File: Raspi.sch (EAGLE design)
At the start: 4 parts

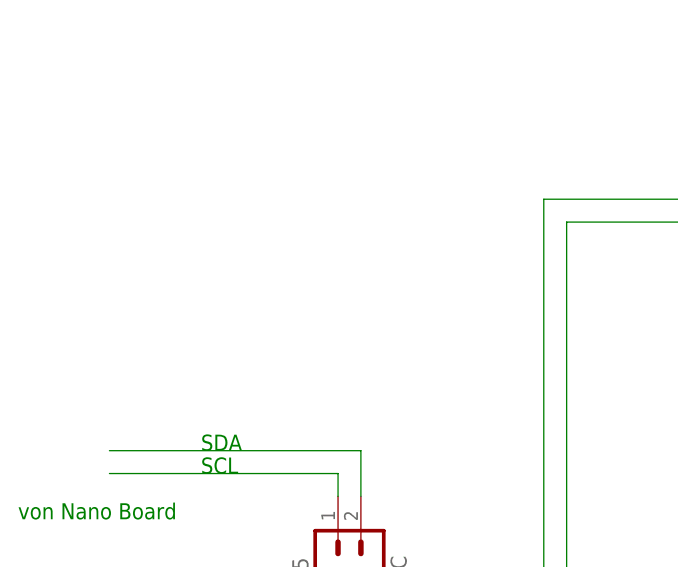
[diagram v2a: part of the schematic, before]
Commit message: 
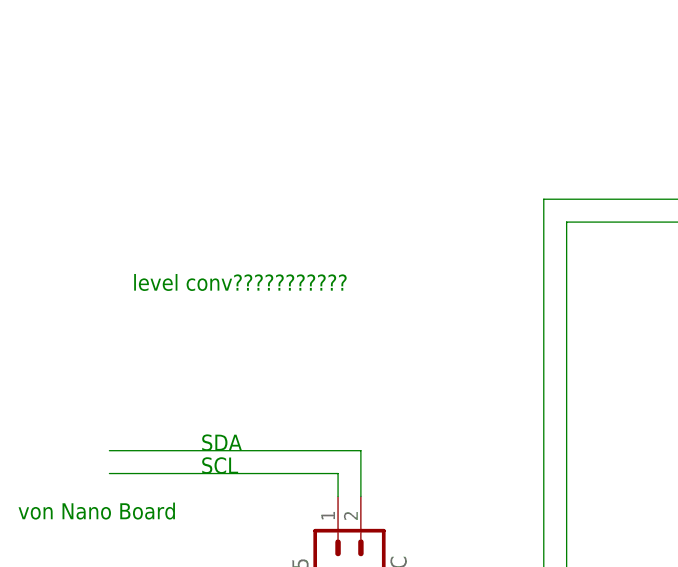
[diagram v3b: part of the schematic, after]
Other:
- note added: "level conv???????????"
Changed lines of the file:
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@@
 <text x="134.62" y="160.02" size="1.778" layer="91" rot="R180">motRechts rückw</text>
 <text x="134.62" y="157.48" size="1.778" layer="91" rot="R180">motRechts PWM</text>
+<text x="-10.16" y="165.1" size="1.778" layer="91">level conv???????????</text>
 </plain>
 <instances>

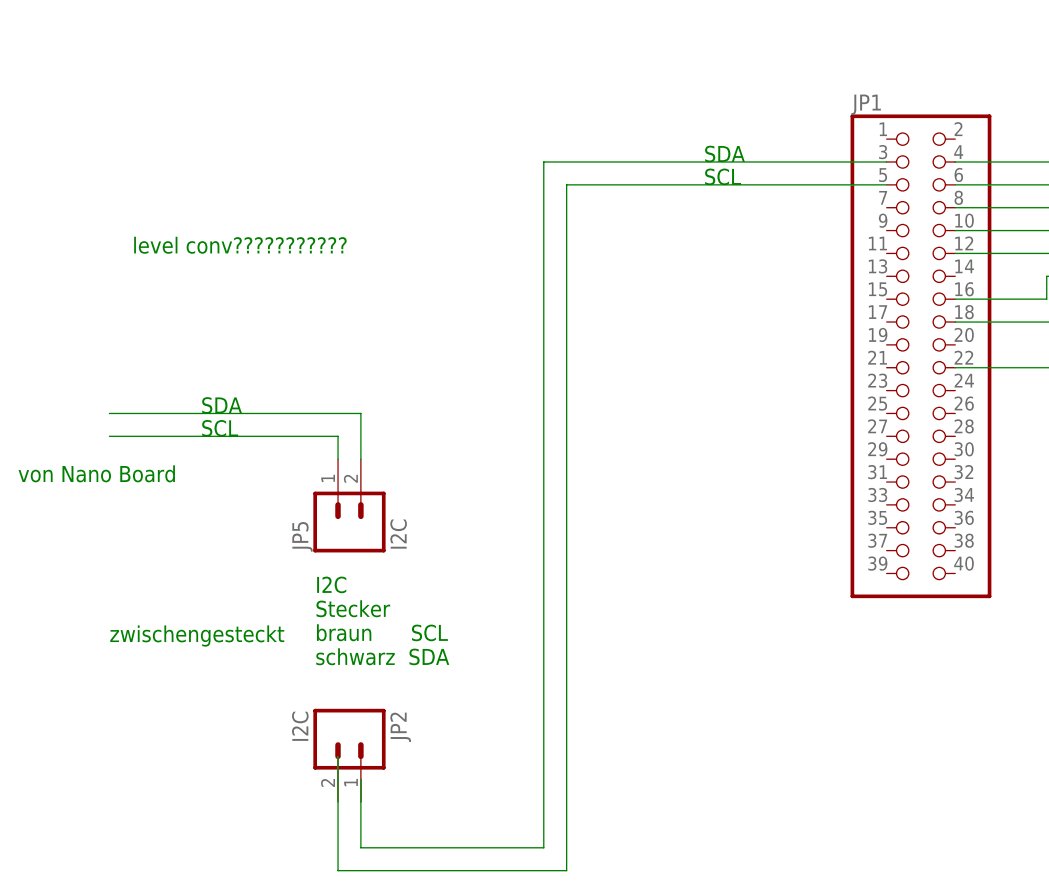
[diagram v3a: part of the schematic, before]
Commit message: 
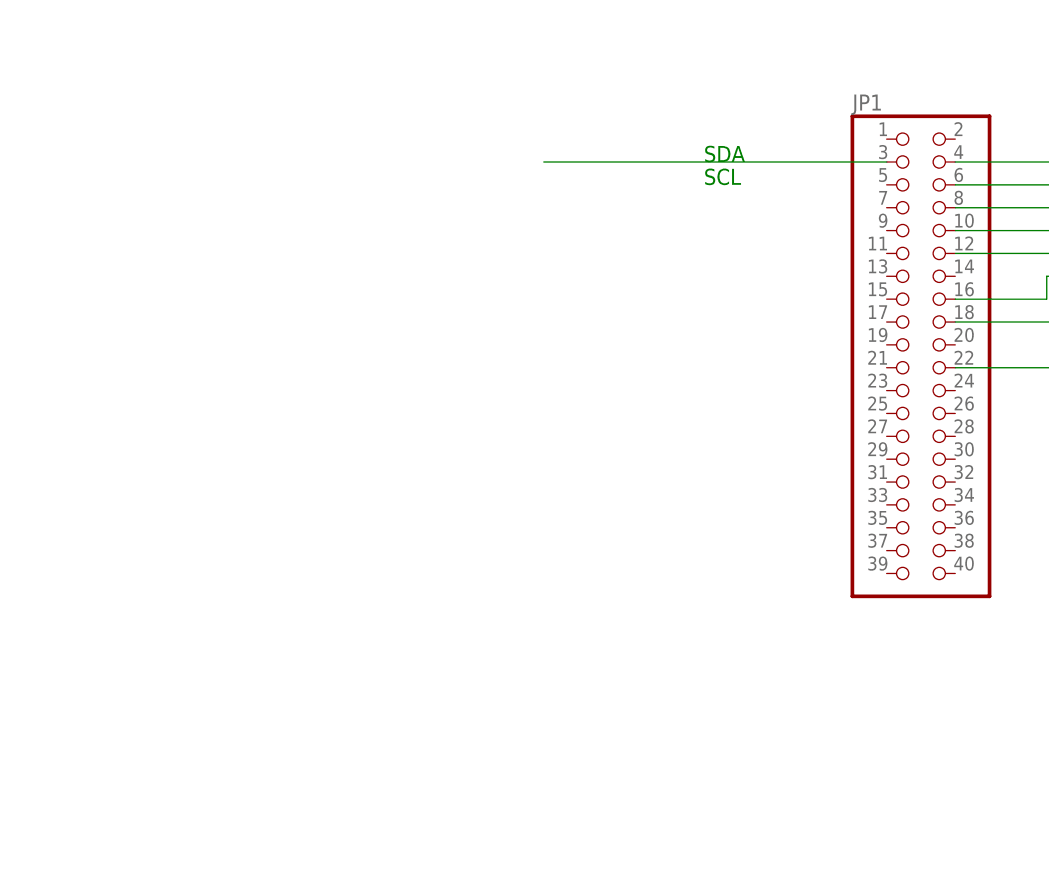
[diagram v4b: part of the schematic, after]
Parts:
- removed JP2, JP5: I2C, SparkFun-Connectors:M02-JST-2MM-SMT
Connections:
- removed net N$10: JP5.2
- removed net N$11: JP5.1
- removed net N$2: JP1.5
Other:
- note removed: "I2C Stecker braun SCL schwarz SDA"
- note removed: "level conv???????????"
- note removed: "von Nano Board"
- note removed: "zwischengesteckt"
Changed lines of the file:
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@@
 <part name="FRAME1" library="SparkFun-Aesthetics" deviceset="FRAME-A4L" device=""/>
 <part name="JP1" library="adafruit" deviceset="PINHD-2X20" device=""/>
-<part name="JP5" library="SparkFun-Connectors" deviceset="M02" device="-JST-2MM-SMT" value="I2C"/>
-<part name="JP2" library="SparkFun-Connectors" deviceset="M02" device="-JST-2MM-SMT" value="I2C"/>
 <part name="JP3" library="SparkFun-Connectors" deviceset="M06" device="LOCK" value="Motorregler"/>
 </parts>
@@
 <sheet>
 <plain>
-<text x="-2.54" y="144.78" size="1.778" layer="91">SCL</text>
-<text x="-2.54" y="147.32" size="1.778" layer="91">SDA</text>
-<text x="10.16" y="119.38" size="1.778" layer="91">I2C
-Stecker
-braun      SCL
-schwarz  SDA</text>
 <text x="53.34" y="175.26" size="1.778" layer="91">SDA</text>
 <text x="53.34" y="172.72" size="1.778" layer="91">SCL</text>
-<text x="-22.86" y="139.7" size="1.778" layer="91">von Nano Board</text>
-<text x="-12.7" y="121.92" size="1.778" layer="91">zwischengesteckt</text>
 <text x="91.44" y="205.74" size="1.778" layer="91">5V</text>
 <text x="96.52" y="205.74" size="1.778" layer="91">GND</text>
@@
 <text x="134.62" y="160.02" size="1.778" layer="91" rot="R180">motRechts rückw</text>
 <text x="134.62" y="157.48" size="1.778" layer="91" rot="R180">motRechts PWM</text>
-<text x="-10.16" y="165.1" size="1.778" layer="91">level conv???????????</text>
 </plain>
 <instances>
 <instance part="FRAME1" gate="G$1" x="-35.56" y="58.42"/>
 <instance part="JP1" gate="A" x="76.2" y="154.94"/>
-<instance part="JP5" gate="G$1" x="15.24" y="134.62" rot="R90"/>
-<instance part="JP2" gate="G$1" x="12.7" y="111.76" rot="R270"/>
 <instance part="JP3" gate="G$1" x="109.22" y="165.1" rot="R180"/>
 </instances>
@@
 </busses>
 <nets>
-<net name="N$10" class="0">
-<segment>
-<wire x1="12.7" y1="144.78" x2="12.7" y2="142.24" width="0.1524" layer="91"/>
-<pinref part="JP5" gate="G$1" pin="2"/>
-<wire x1="-12.7" y1="144.78" x2="12.7" y2="144.78" width="0.1524" layer="91"/>
-</segment>
-</net>
-<net name="N$11" class="0">
-<segment>
-<wire x1="-12.7" y1="147.32" x2="15.24" y2="147.32" width="0.1524" layer="91"/>
-<wire x1="15.24" y1="147.32" x2="15.24" y2="142.24" width="0.1524" layer="91"/>
-<pinref part="JP5" gate="G$1" pin="1"/>
-</segment>
-</net>
 <net name="N$1" class="0">
 <segment>
 <pinref part="JP1" gate="A" pin="3"/>
 <wire x1="73.66" y1="175.26" x2="35.56" y2="175.26" width="0.1524" layer="91"/>
-<wire x1="35.56" y1="175.26" x2="35.56" y2="99.06" width="0.1524" layer="91"/>
-<wire x1="35.56" y1="99.06" x2="15.24" y2="99.06" width="0.1524" layer="91"/>
-<wire x1="15.24" y1="99.06" x2="15.24" y2="106.68" width="0.1524" layer="91"/>
-</segment>
-</net>
-<net name="N$2" class="0">
-<segment>
-<pinref part="JP1" gate="A" pin="5"/>
-<wire x1="73.66" y1="172.72" x2="38.1" y2="172.72" width="0.1524" layer="91"/>
-<wire x1="38.1" y1="172.72" x2="38.1" y2="96.52" width="0.1524" layer="91"/>
-<wire x1="38.1" y1="96.52" x2="12.7" y2="96.52" width="0.1524" layer="91"/>
-<wire x1="12.7" y1="96.52" x2="12.7" y2="109.22" width="0.1524" layer="91"/>
 </segment>
 </net>
@@
 </schematic>
 </drawing>
-<compatibility>
-<note version="6.3" minversion="6.2.2" severity="warning">
-Since Version 6.2.2 text objects can contain more than one line,
-which will not be processed correctly with this version.
-</note>
-</compatibility>
 </eagle>

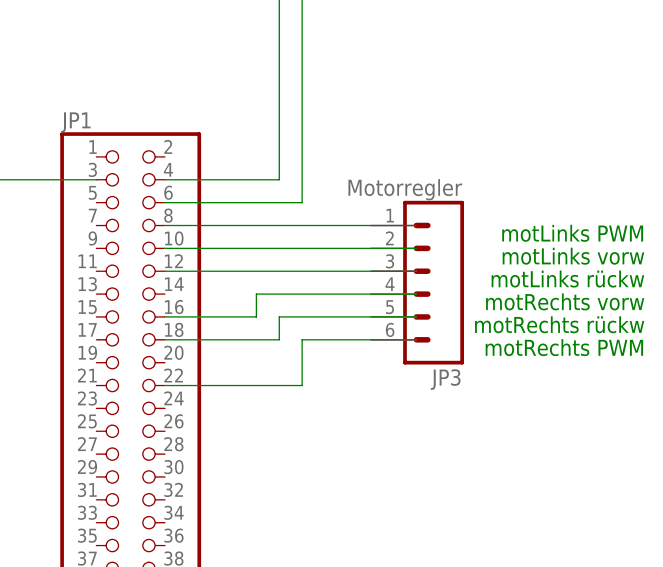
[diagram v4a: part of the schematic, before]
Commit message: 
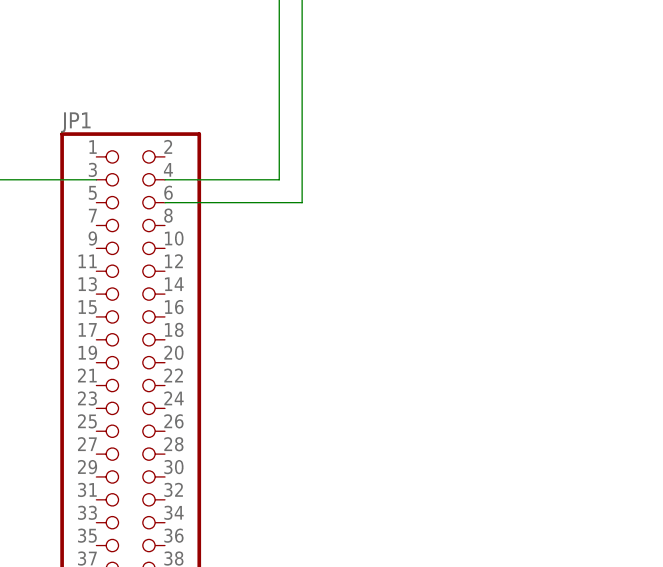
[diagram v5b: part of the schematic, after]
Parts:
- removed JP3: Motorregler, SparkFun-Connectors:M06LOCK
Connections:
- removed net N$12: JP1.22
- removed net N$5: JP1.8
- removed net N$6: JP1.10
- removed net N$7: JP1.12
- removed net N$8: JP1.16
- removed net N$9: JP1.18
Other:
- note removed: "motLinks PWM"
- note removed: "motLinks rückw"
- note removed: "motLinks vorw"
- note removed: "motRechts PWM"
- note removed: "motRechts rückw"
- note removed: "motRechts vorw"
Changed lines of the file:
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@@
 <part name="FRAME1" library="SparkFun-Aesthetics" deviceset="FRAME-A4L" device=""/>
 <part name="JP1" library="adafruit" deviceset="PINHD-2X20" device=""/>
-<part name="JP3" library="SparkFun-Connectors" deviceset="M06" device="LOCK" value="Motorregler"/>
 </parts>
 <sheets>
@@
 <text x="96.52" y="205.74" size="1.778" layer="91">GND</text>
 <text x="88.9" y="213.36" size="1.778" layer="91">zur spgsplatine</text>
-<text x="134.62" y="170.18" size="1.778" layer="91" rot="R180">motLinks PWM</text>
-<text x="134.62" y="167.64" size="1.778" layer="91" rot="R180">motLinks vorw</text>
-<text x="134.62" y="165.1" size="1.778" layer="91" rot="R180">motLinks rückw</text>
-<text x="134.62" y="162.56" size="1.778" layer="91" rot="R180">motRechts vorw</text>
-<text x="134.62" y="160.02" size="1.778" layer="91" rot="R180">motRechts rückw</text>
-<text x="134.62" y="157.48" size="1.778" layer="91" rot="R180">motRechts PWM</text>
 </plain>
 <instances>
 <instance part="FRAME1" gate="G$1" x="-35.56" y="58.42"/>
 <instance part="JP1" gate="A" x="76.2" y="154.94"/>
-<instance part="JP3" gate="G$1" x="109.22" y="165.1" rot="R180"/>
 </instances>
 <busses>
@@
 </segment>
 </net>
-<net name="N$5" class="0">
-<segment>
-<pinref part="JP1" gate="A" pin="8"/>
-<wire x1="81.28" y1="170.18" x2="109.22" y2="170.18" width="0.1524" layer="91"/>
-</segment>
-</net>
-<net name="N$6" class="0">
-<segment>
-<pinref part="JP1" gate="A" pin="10"/>
-<wire x1="81.28" y1="167.64" x2="109.22" y2="167.64" width="0.1524" layer="91"/>
-</segment>
-</net>
-<net name="N$8" class="0">
-<segment>
-<pinref part="JP1" gate="A" pin="16"/>
-<wire x1="81.28" y1="160.02" x2="91.44" y2="160.02" width="0.1524" layer="91"/>
-<wire x1="91.44" y1="160.02" x2="91.44" y2="162.56" width="0.1524" layer="91"/>
-<wire x1="91.44" y1="162.56" x2="109.22" y2="162.56" width="0.1524" layer="91"/>
-</segment>
-</net>
-<net name="N$9" class="0">
-<segment>
-<pinref part="JP1" gate="A" pin="18"/>
-<wire x1="81.28" y1="157.48" x2="93.98" y2="157.48" width="0.1524" layer="91"/>
-<wire x1="93.98" y1="157.48" x2="93.98" y2="160.02" width="0.1524" layer="91"/>
-<wire x1="93.98" y1="160.02" x2="109.22" y2="160.02" width="0.1524" layer="91"/>
-</segment>
-</net>
-<net name="N$12" class="0">
-<segment>
-<wire x1="96.52" y1="152.4" x2="96.52" y2="157.48" width="0.1524" layer="91"/>
-<wire x1="96.52" y1="157.48" x2="109.22" y2="157.48" width="0.1524" layer="91"/>
-<pinref part="JP1" gate="A" pin="22"/>
-<wire x1="81.28" y1="152.4" x2="96.52" y2="152.4" width="0.1524" layer="91"/>
-</segment>
-</net>
-<net name="N$7" class="0">
-<segment>
-<pinref part="JP1" gate="A" pin="12"/>
-<wire x1="81.28" y1="165.1" x2="109.22" y2="165.1" width="0.1524" layer="91"/>
-</segment>
-</net>
